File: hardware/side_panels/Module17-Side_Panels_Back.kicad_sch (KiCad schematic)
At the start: 5 parts

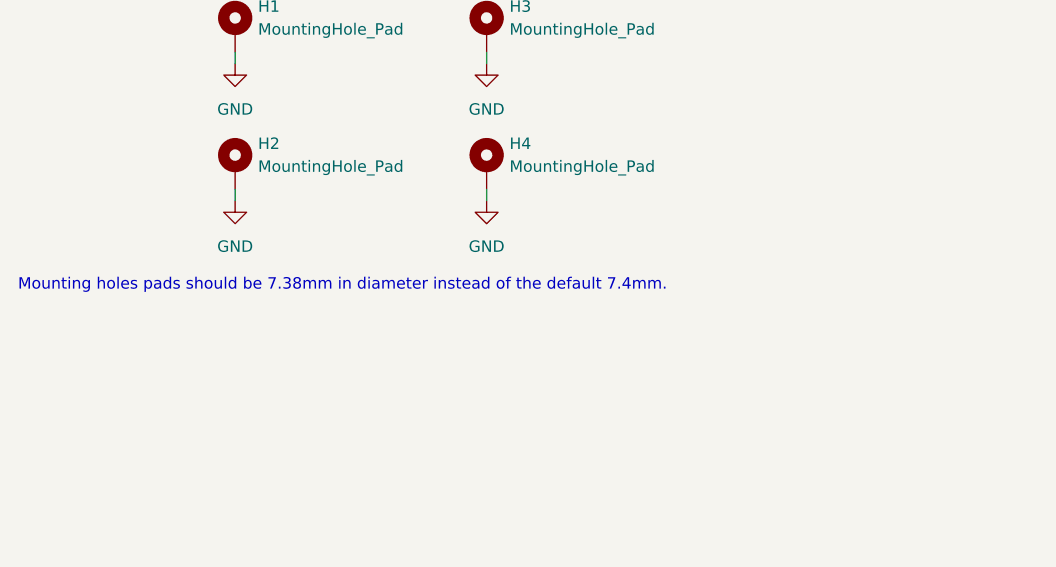
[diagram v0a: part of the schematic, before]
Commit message: Updated Side Panels to Rev 0.99b
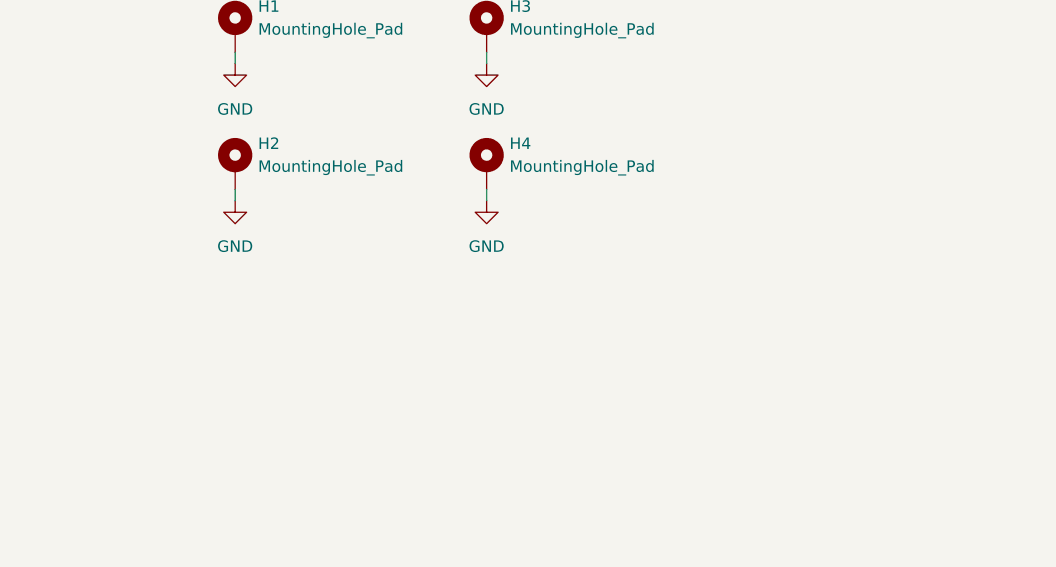
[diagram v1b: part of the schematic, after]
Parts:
- H1, H2, H3, H4: footprint MountingHole:MountingHole_3.7mm_Pad_Via -> M17_mounting_hole:MountingHole_3.7mm_Pad_Via_Small_Pad
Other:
- note removed: "Mounting holes pads should be 7.38mm in diameter instead of the default 7.4mm."

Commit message: Updated side panels PCBs to revision 1.0
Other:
- company: (none) -> M17 Project
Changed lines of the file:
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@@
 	(title_block
 		(title "Module17 HMI Back Panel")
-		(date "2024-01-11")
-		(rev "Rev 0.99")
+		(date "2024-06-19")
+		(rev "Rev 1.0")
+		(company "M17 Project")
 		(comment 1 "Morgan ON4MOD")
+		(comment 2 "Authors:")
 	)
 	(wire
